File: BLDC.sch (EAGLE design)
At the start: 122 parts, among them Q1 IRFS7530TRLPBF, Q2 IRFS7530TRLPBF, Q3 IRFS7530TRLPBF, Q4 IRFS7530TRLPBF, Q5 IRFS7530TRLPBF, Q6 IRFS7530TRLPBF, U1 DRV8302, U102 LM3671MF-3.3/NOPB, U104 MCP2562, U2 STM32F405RGT6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

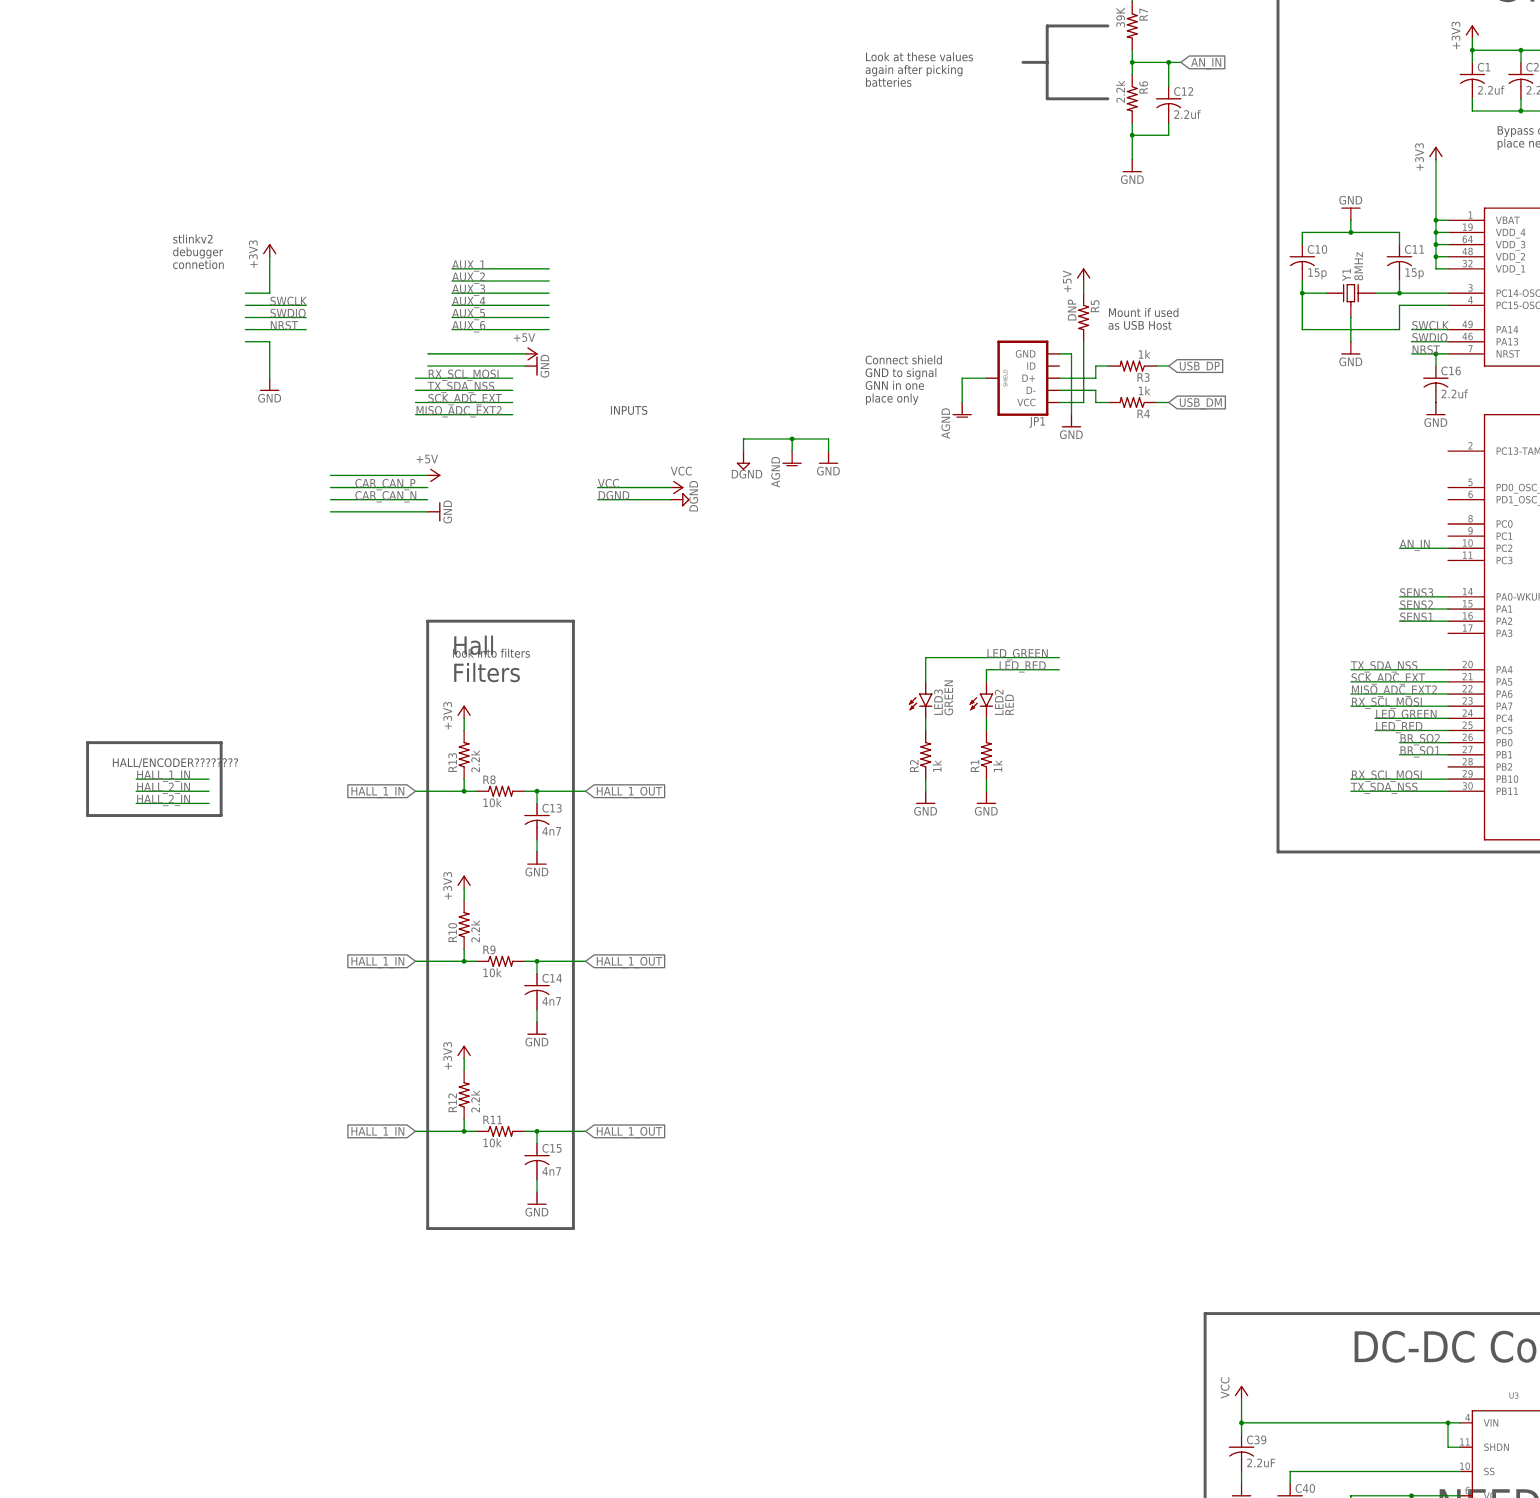
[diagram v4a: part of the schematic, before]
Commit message: added brd temp and motor temp
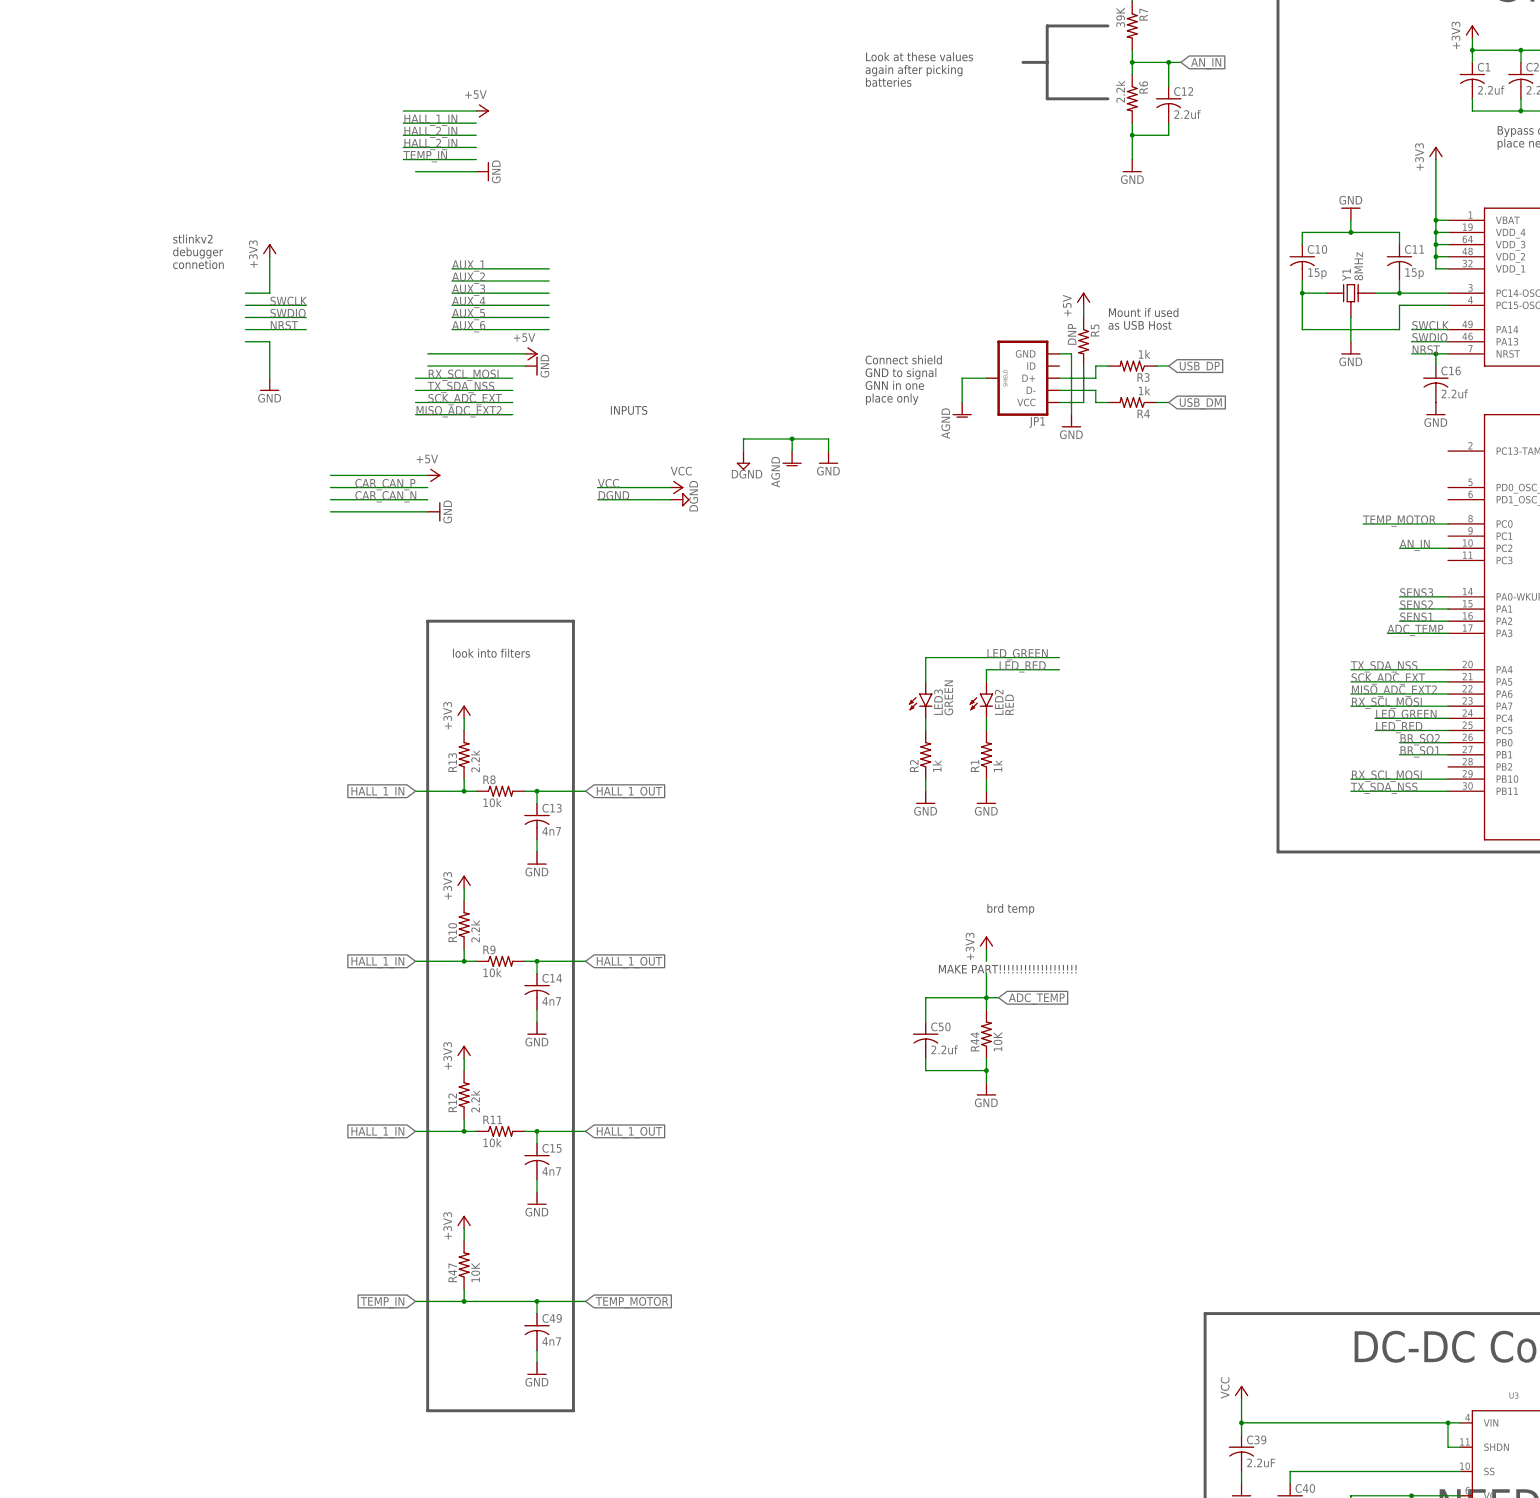
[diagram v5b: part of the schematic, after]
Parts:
- added C49: 4n7, rcl:C-USC0805
- added C50: 2.2uf, rcl:C-USC0805
- added R44, R47: 10K, adafruit:R-US_R0805
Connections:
- new net ADC_TEMP: C50.1, R44.2, U2.PA3
- new net TEMP_IN: R47.1
- new net TEMP_MOTOR: C49.1, U2.PC0
- net +3V3: now also R47.2
- net GND: now also C49.2, C50.2, R44.1
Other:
- note added: "MAKE PART!!!!!!!!!!!!!!!!!!!"
- note added: "brd temp"
- note removed: "HALL/ENCODER????????"
- note removed: "Hall Filters"
- moved on the sheet: R5

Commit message: cleaned up sch a bit
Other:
- note added: "Need output connect"
- moved on the sheet: C109, C110, C115, C116, C13, C14, C15, C17, C18, C19, C20, C21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

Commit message: added pin headeders and 60V shtky diode
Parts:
- added D3: CD1206-B260, FormE:CD1206-B260
- added J1: J_1X4, FormE:J_1X4
- added J2: J_1X6, FormE:J_1X6
- added J3: J_1X7, FormE:J_1X7
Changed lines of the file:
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@@
 <part name="P+16" library="supply1" deviceset="+5V" device=""/>
 <part name="GND45" library="supply1" deviceset="GND" device=""/>
+<part name="J1" library="FormE" deviceset="J_1X4" device=""/>
+<part name="J2" library="FormE" deviceset="J_1X6" device=""/>
+<part name="J3" library="FormE" deviceset="J_1X7" device=""/>
+<part name="D3" library="FormE" deviceset="CD1206-B260" device=""/>
 </parts>
 <sheets>
@@
 <instance part="P+16" gate="1" x="-246.38" y="66.04" rot="R270"/>
 <instance part="GND45" gate="1" x="-246.38" y="53.34" rot="R90"/>
+<instance part="J1" gate="G$1" x="-337.82" y="48.26"/>
+<instance part="J2" gate="G$1" x="-337.82" y="25.4"/>
+<instance part="J3" gate="G$1" x="-332.74" y="-7.62"/>
+<instance part="D3" gate="G$1" x="251.46" y="40.64"/>
 </instances>
 <busses>

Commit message: connected inputs
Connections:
- new net HALL_2_IN: J2.4
- new net HALL_3_IN: J2.3
- net +3V3: now also J3.6
- net +5V: now also J1.4, J2.6, J3.7
- net CAR_CAN_N: now also J1.2
- net CAR_CAN_P: now also J1.3
- net GND: now also D3.A, J1.1, J2.1, J3.1
- net HALL_1_IN: now also J2.5
- net MISO_ADC_EXT2: now also J3.2
- net N$21: now also D3.K
- net RX_SCL_MOSI: now also J3.5
- net SCK_ADC_EXT: now also J3.3
- net TEMP_IN: now also J2.2
- net TX_SDA_NSS: now also J3.4
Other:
- note removed: "DIODE!!!!!!!!!!!!!!!!!"
- moved on the sheet: D3, J1, J2, J3
